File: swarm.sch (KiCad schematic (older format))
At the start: 22 parts, among them P1 USB_OTG, SW1 SW_PUSH, U1 STM32F103RETx, U2 LM3671MF-3.3, Y1 Crystal

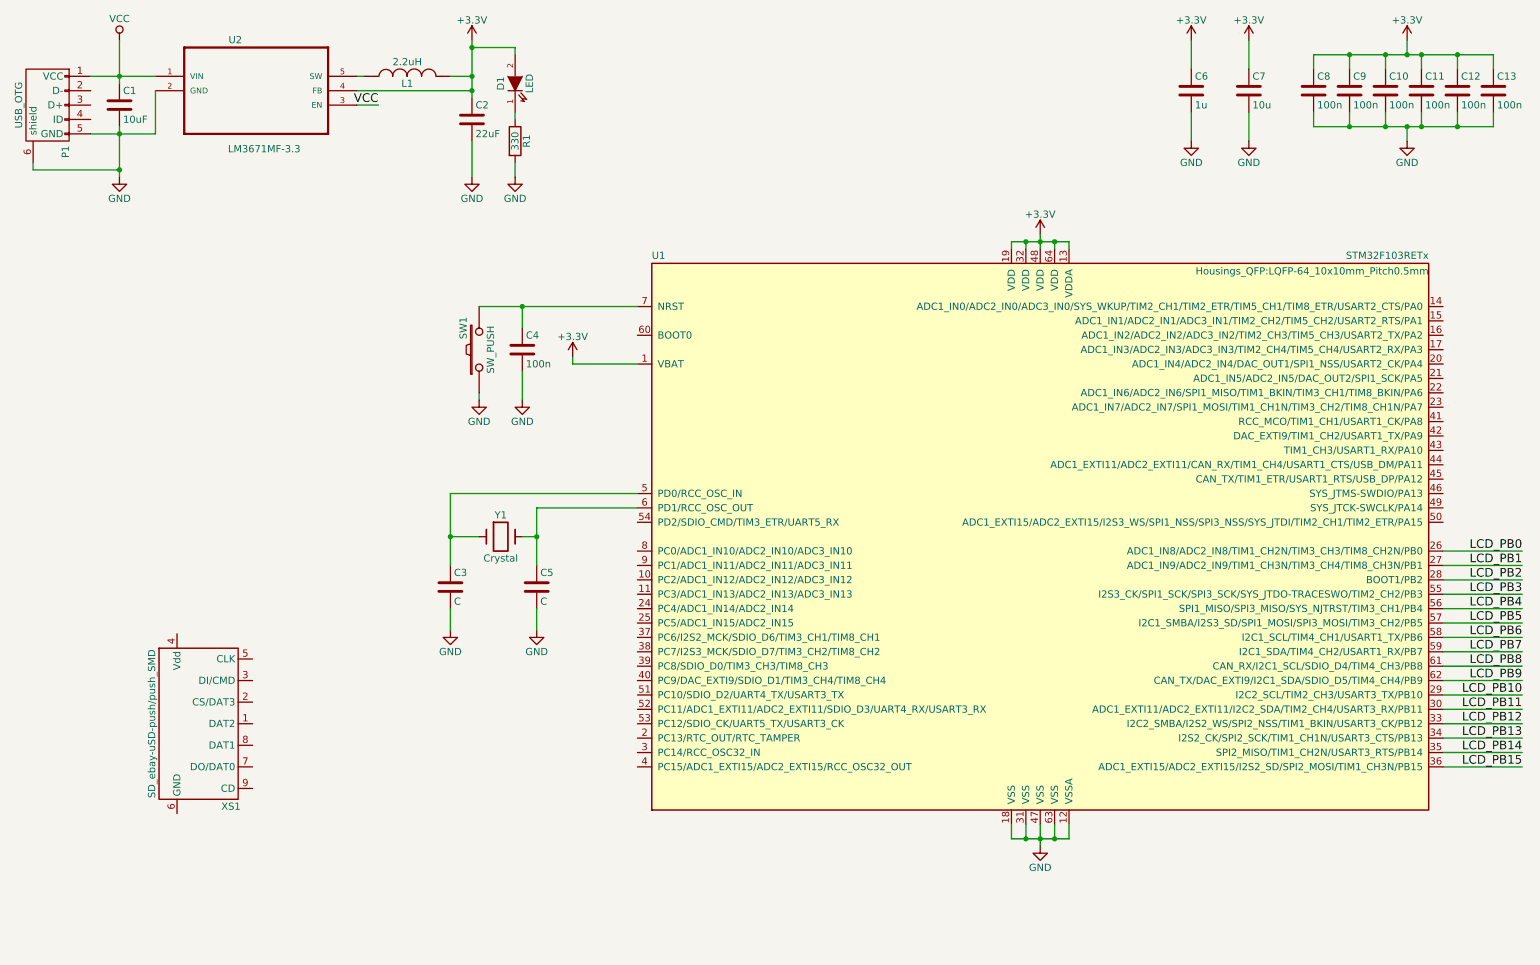
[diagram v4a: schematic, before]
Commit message: Adds Micro SD card socket connection
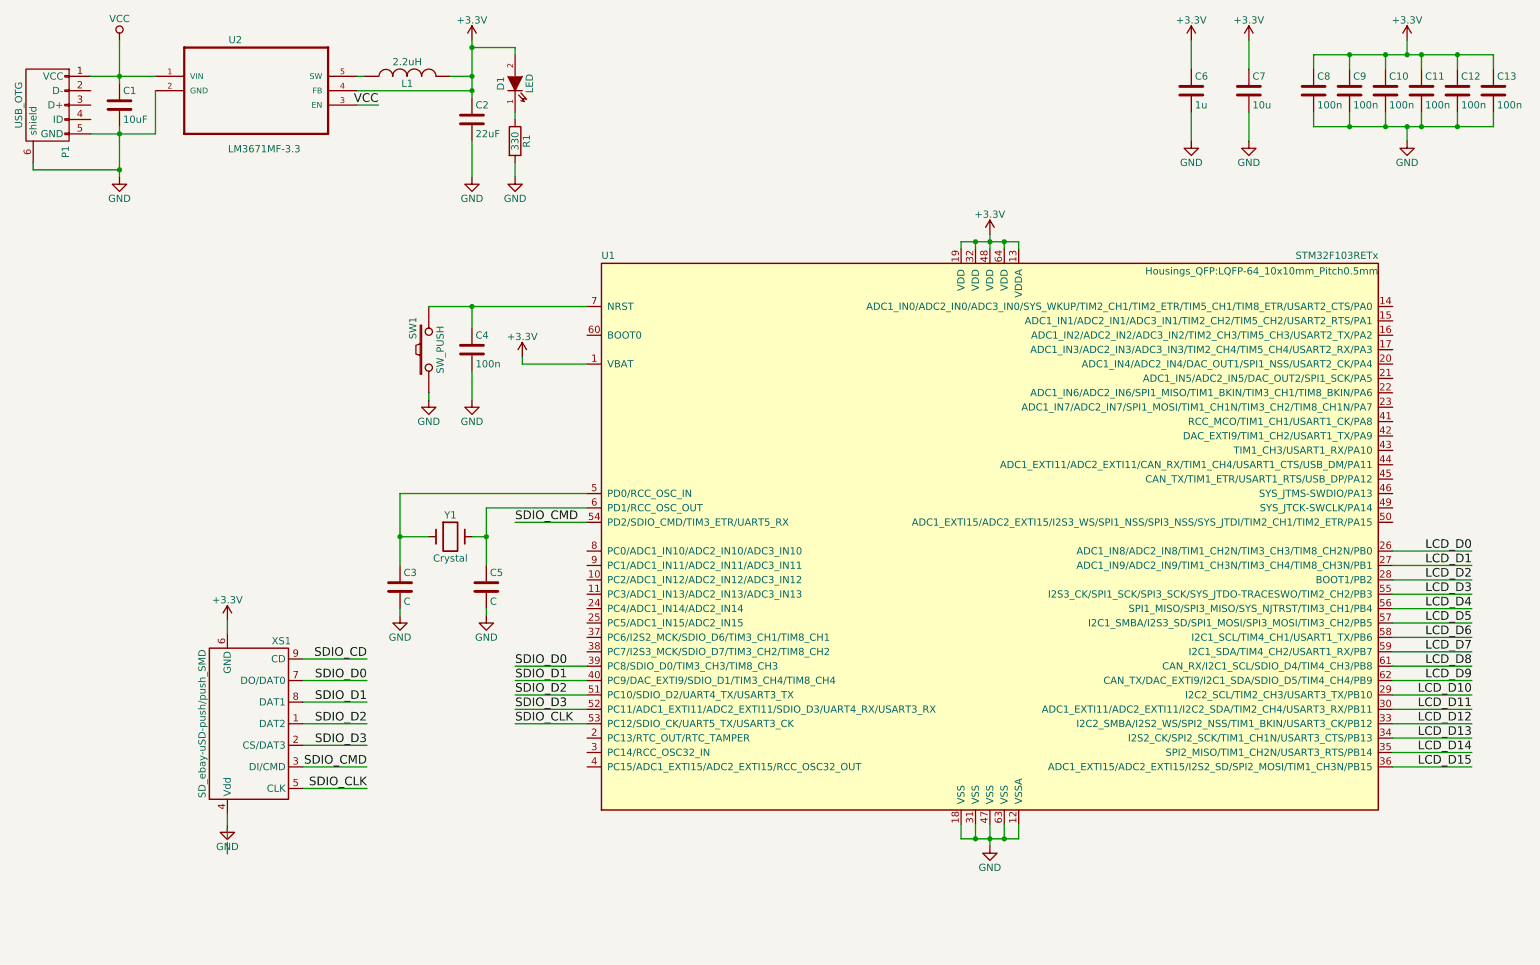
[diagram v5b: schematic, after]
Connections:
- net labels added: LCD_D0, LCD_D1, LCD_D10, LCD_D11, LCD_D12, LCD_D13, LCD_D14, LCD_D15, LCD_D2, LCD_D3, LCD_D4, LCD_D5, LCD_D6, LCD_D7, LCD_D8, LCD_D9, SDIO_CD, SDIO_CLK, SDIO_CMD, SDIO_D0, SDIO_D1, SDIO_D2, SDIO_D3
- net labels removed: LCD_PB0, LCD_PB1, LCD_PB10, LCD_PB11, LCD_PB12, LCD_PB13, LCD_PB14, LCD_PB15, LCD_PB2, LCD_PB3, LCD_PB4, LCD_PB5, LCD_PB6, LCD_PB7, LCD_PB8, LCD_PB9
- wire segments 79 -> 96
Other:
- moved on the sheet: C3, C4, C5, SW1, U1, XS1, Y1

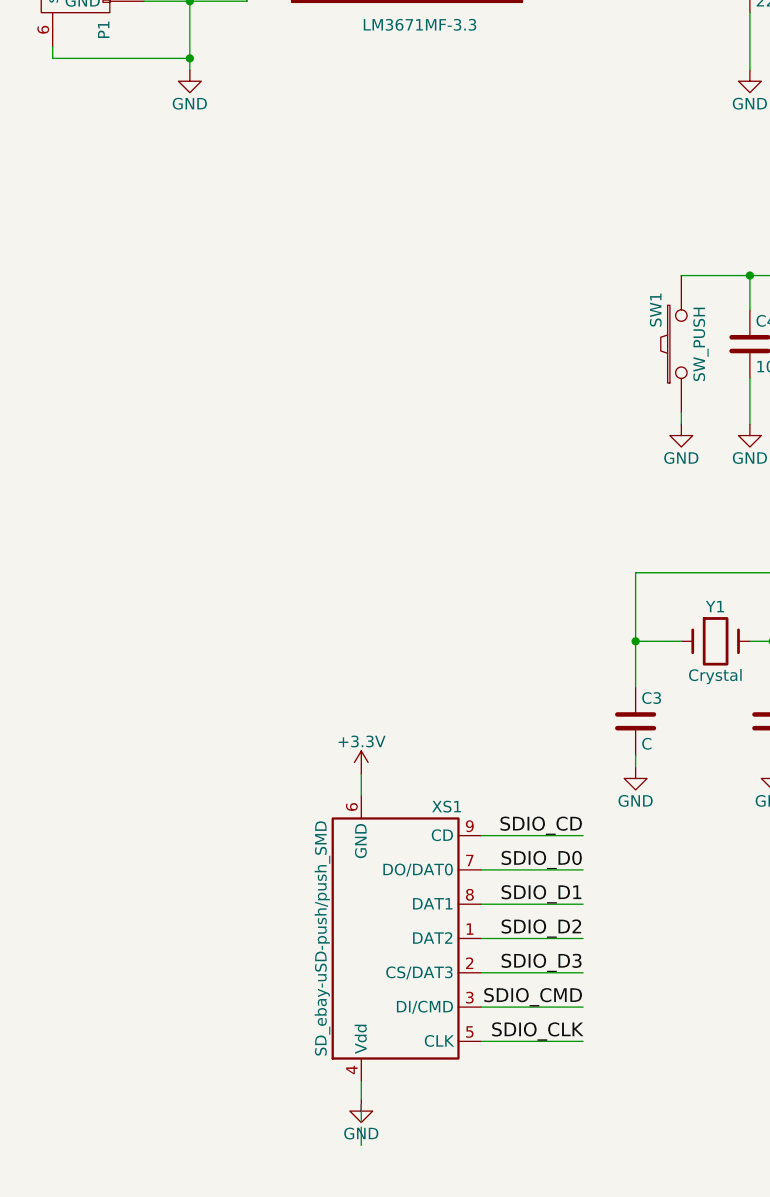
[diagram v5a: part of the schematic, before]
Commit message: Adds LCD connector 2x20 pins
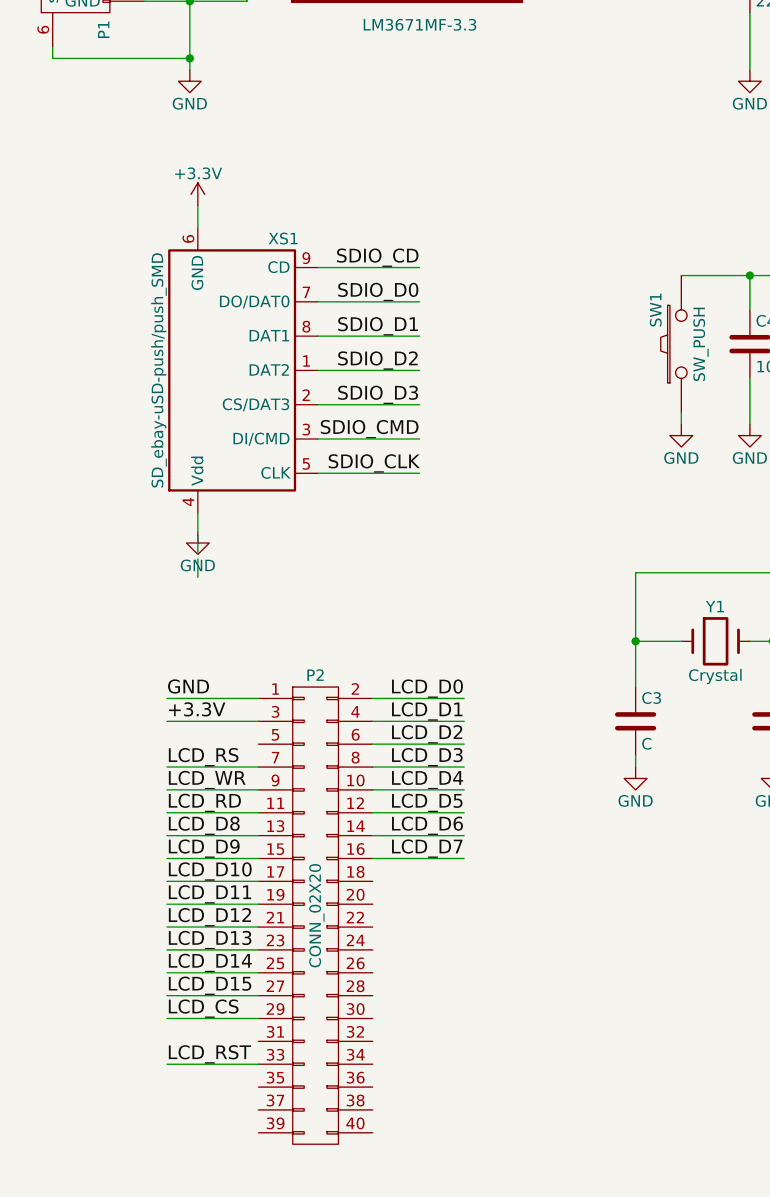
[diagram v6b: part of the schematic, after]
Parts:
- added P2: CONN_02X20, Pin_Headers:Pin_Header_Straight_2x20, symbol CONN_02X20
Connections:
- net labels added: LCD_CS, LCD_RD, LCD_RS, LCD_RST, LCD_WR
- wire segments 96 -> 119
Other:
- moved on the sheet: XS1
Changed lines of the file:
@@
 L SD_ebay-uSD-push/push_SMD XS1
 U 1 1 5840E1A5
-P 2300 5500
-F 0 "XS1" H 2525 4925 50  0000 C CNN
-F 1 "SD_ebay-uSD-push/push_SMD" V 1975 5500 50  0000 C CNN
-F 2 "volium:Conn_uSDcard" H 2300 5550 10  0001 C CNN
-F 3 "https://wiki.microduino.cc/images/c/ca/MicroSD.pdf" H 2300 5440 10  0001 C CNN
-F 4 "_" H 2300 5410 10  0001 C CNN "Manf#"
-F 5 "ebay" H 2300 5500 10  0001 C CNN "Manf"
-	1    2300 5500
+P 1585 3015
+F 0 "XS1" H 1810 2440 50  0000 C CNN
+F 1 "SD_ebay-uSD-push/push_SMD" V 1260 3015 50  0000 C CNN
+F 2 "volium:Conn_uSDcard" H 1585 3065 10  0001 C CNN
+F 3 "https://wiki.microduino.cc/images/c/ca/MicroSD.pdf" H 1585 2955 10  0001 C CNN
+F 4 "_" H 1585 2925 10  0001 C CNN "Manf#"
+F 5 "ebay" H 1585 3015 10  0001 C CNN "Manf"
+	1    1585 3015
 	1    0    0    1
 $EndComp
@@
 	4650 4100 4150 4100
 Wire Wire Line
-	2675 5050 3120 5050
-Text Label 3120 5950 2    60   ~ 0
+	1960 2565 2405 2565
+Text Label 2405 3465 2    60   ~ 0
 SDIO_CLK
 Wire Wire Line
-	2675 5200 3120 5200
-Wire Wire Line
-	2675 5350 3120 5350
-Wire Wire Line
-	2675 5500 3120 5500
-Wire Wire Line
-	2675 5650 3120 5650
-Wire Wire Line
-	2675 5800 3120 5800
-Wire Wire Line
-	2675 5950 3120 5950
-Text Label 3120 5200 2    60   ~ 0
+	1960 2715 2405 2715
+Wire Wire Line
+	1960 2865 2405 2865
+Wire Wire Line
+	1960 3015 2405 3015
+Wire Wire Line
+	1960 3165 2405 3165
+Wire Wire Line
+	1960 3315 2405 3315
+Wire Wire Line
+	1960 3465 2405 3465
+Text Label 2405 2715 2    60   ~ 0
 SDIO_D0
-Text Label 3120 5350 2    60   ~ 0
+Text Label 2405 2865 2    60   ~ 0
 SDIO_D1
-Text Label 3120 5500 2    60   ~ 0
+Text Label 2405 3015 2    60   ~ 0
 SDIO_D2
-Text Label 3120 5650 2    60   ~ 0
+Text Label 2405 3165 2    60   ~ 0
 SDIO_D3
-Text Label 3120 5800 2    60   ~ 0
+Text Label 2405 3315 2    60   ~ 0
 SDIO_CMD
-Text Label 3120 5050 2    60   ~ 0
+Text Label 2405 2565 2    60   ~ 0
 SDIO_CD
 $Comp
 L +3.3V #PWR019
 U 1 1 58424C6C
-P 2150 4780
-F 0 "#PWR019" H 2150 4630 50  0001 C CNN
-F 1 "+3.3V" H 2150 4920 50  0000 C CNN
-F 2 "" H 2150 4780 50  0000 C CNN
-F 3 "" H 2150 4780 50  0000 C CNN
-	1    2150 4780
+P 1435 2295
+F 0 "#PWR019" H 1435 2145 50  0001 C CNN
+F 1 "+3.3V" H 1435 2435 50  0000 C CNN
+F 2 "" H 1435 2295 50  0000 C CNN
+F 3 "" H 1435 2295 50  0000 C CNN
+	1    1435 2295
 	1    0    0    -1
 $EndComp
 Wire Wire Line
-	2150 4780 2150 4875
+	1435 2295 1435 2390
 $Comp
 L GND #PWR020
 U 1 1 5842512A
-P 2150 6205
-F 0 "#PWR020" H 2150 5955 50  0001 C CNN
-F 1 "GND" H 2150 6055 50  0000 C CNN
-F 2 "" H 2150 6205 50  0000 C CNN
-F 3 "" H 2150 6205 50  0000 C CNN
-	1    2150 6205
+P 1435 3720
+F 0 "#PWR020" H 1435 3470 50  0001 C CNN
+F 1 "GND" H 1435 3570 50  0000 C CNN
+F 2 "" H 1435 3720 50  0000 C CNN
+F 3 "" H 1435 3720 50  0000 C CNN
+	1    1435 3720
 	1    0    0    -1
 $EndComp
 Wire Wire Line
-	2150 6205 2150 6125
-Wire Wire Line
-	2150 6305 2150 6225
-Wire Wire Line
-	2150 6405 2150 6325
+	1435 3720 1435 3640
+Wire Wire Line
+	1435 3820 1435 3740
+Wire Wire Line
+	1435 3920 1435 3840
+$Comp
+L CONN_02X20 P2
+U 1 1 58432580
+P 1950 5400
+F 0 "P2" H 1950 6450 50  0000 C CNN
+F 1 "CONN_02X20" V 1950 5400 50  0000 C CNN
+F 2 "Pin_Headers:Pin_Header_Straight_2x20" H 1950 4450 50  0001 C CNN
+F 3 "" H 1950 4450 50  0000 C CNN
+	1    1950 5400
+	1    0    0    -1
+$EndComp
+Wire Wire Line
+	1700 4450 1300 4450
+Wire Wire Line
+	2200 4450 2600 4450
+Text Label 2600 4450 2    60   ~ 0
+LCD_D0
+Text Label 2600 4550 2    60   ~ 0
+LCD_D1
+Text Label 2600 4650 2    60   ~ 0
+LCD_D2
+Text Label 2600 4750 2    60   ~ 0
+LCD_D3
+Text Label 2600 4850 2    60   ~ 0
+LCD_D4
+Text Label 2600 4950 2    60   ~ 0
+LCD_D5
+Text Label 2600 5050 2    60   ~ 0
+LCD_D6
+Text Label 2600 5150 2    60   ~ 0
+LCD_D7
+Wire Wire Line
+	2200 4550 2600 4550
+Wire Wire Line
+	2200 4650 2600 4650
+Wire Wire Line
+	2200 4750 2600 4750
+Wire Wire Line
+	2200 4850 2600 4850
+Wire Wire Line
+	2200 4950 2600 4950
+Wire Wire Line
+	2200 5050 2600 5050
+Wire Wire Line
+	2200 5150 2600 5150
+Wire Wire Line
+	1700 5050 1300 5050
+Wire Wire Line
+	1700 5150 1300 5150
+Wire Wire Line
+	1700 5250 1300 5250
+Wire Wire Line
+	1700 5350 1300 5350
+Wire Wire Line
+	1700 5450 1300 5450
+Wire Wire Line
+	1700 5550 1300 5550
+Wire Wire Line
+	1700 5650 1300 5650
+Wire Wire Line
+	1700 5750 1300 5750
+Text Label 1300 5050 0    60   ~ 0
+LCD_D8
+Text Label 1300 5150 0    60   ~ 0
+LCD_D9
+Text Label 1300 5250 0    60   ~ 0
+LCD_D10
+Text Label 1300 5350 0    60   ~ 0
+LCD_D11
+Text Label 1300 5450 0    60   ~ 0
+LCD_D12
+Text Label 1300 5550 0    60   ~ 0
+LCD_D13
+Text Label 1300 5650 0    60   ~ 0
+LCD_D14
+Text Label 1300 5750 0    60   ~ 0
+LCD_D15
+Text Label 1300 4450 0    60   ~ 0
+GND
+Text Label 1300 4550 0    60   ~ 0
++3.3V
+Wire Wire Line
+	1700 4550 1300 4550
+Wire Wire Line
+	1700 4750 1300 4750
+Wire Wire Line
+	1700 4850 1300 4850
+Wire Wire Line
+	1700 4950 1300 4950
+Text Label 1300 4750 0    60   ~ 0
+LCD_RS
+Text Label 1300 4850 0    60   ~ 0
+LCD_WR
+Text Label 1300 4950 0    60   ~ 0
+LCD_RD
+Wire Wire Line
+	1700 5850 1300 5850
+Wire Wire Line
+	1700 6050 1300 6050
+Text Label 1300 5850 0    60   ~ 0
+LCD_CS
+Text Label 1300 6050 0    60   ~ 0
+LCD_RST
 $EndSCHEMATC

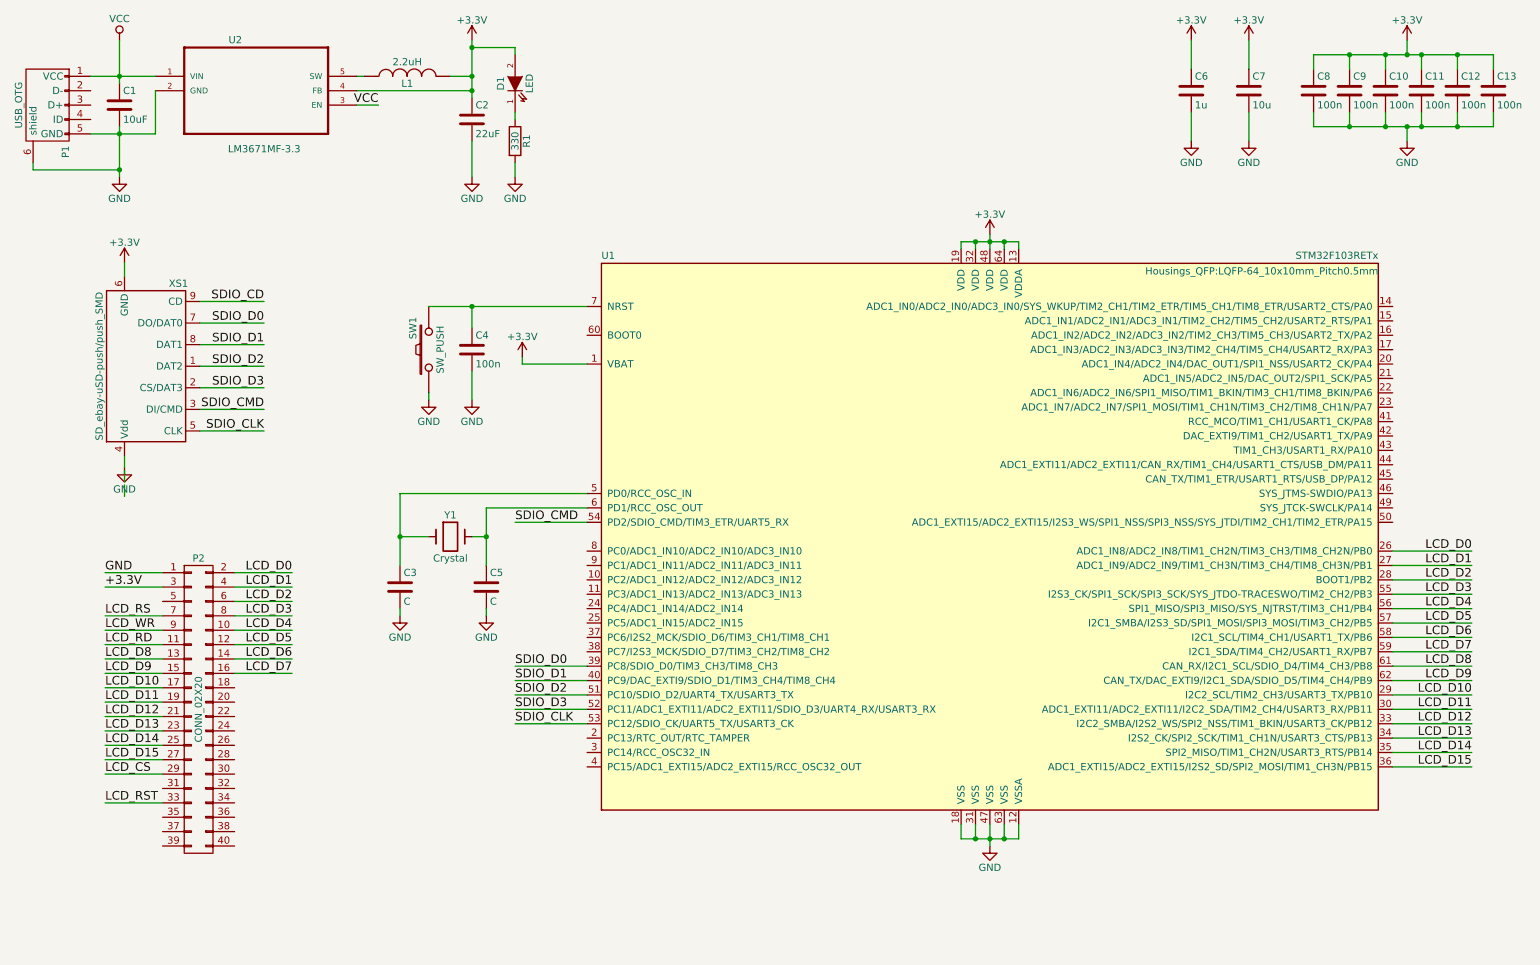
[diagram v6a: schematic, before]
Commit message: Adds Serial Wire Debug connector (5 pins) Sets up PCB layers based on Osh Park's Layer setup
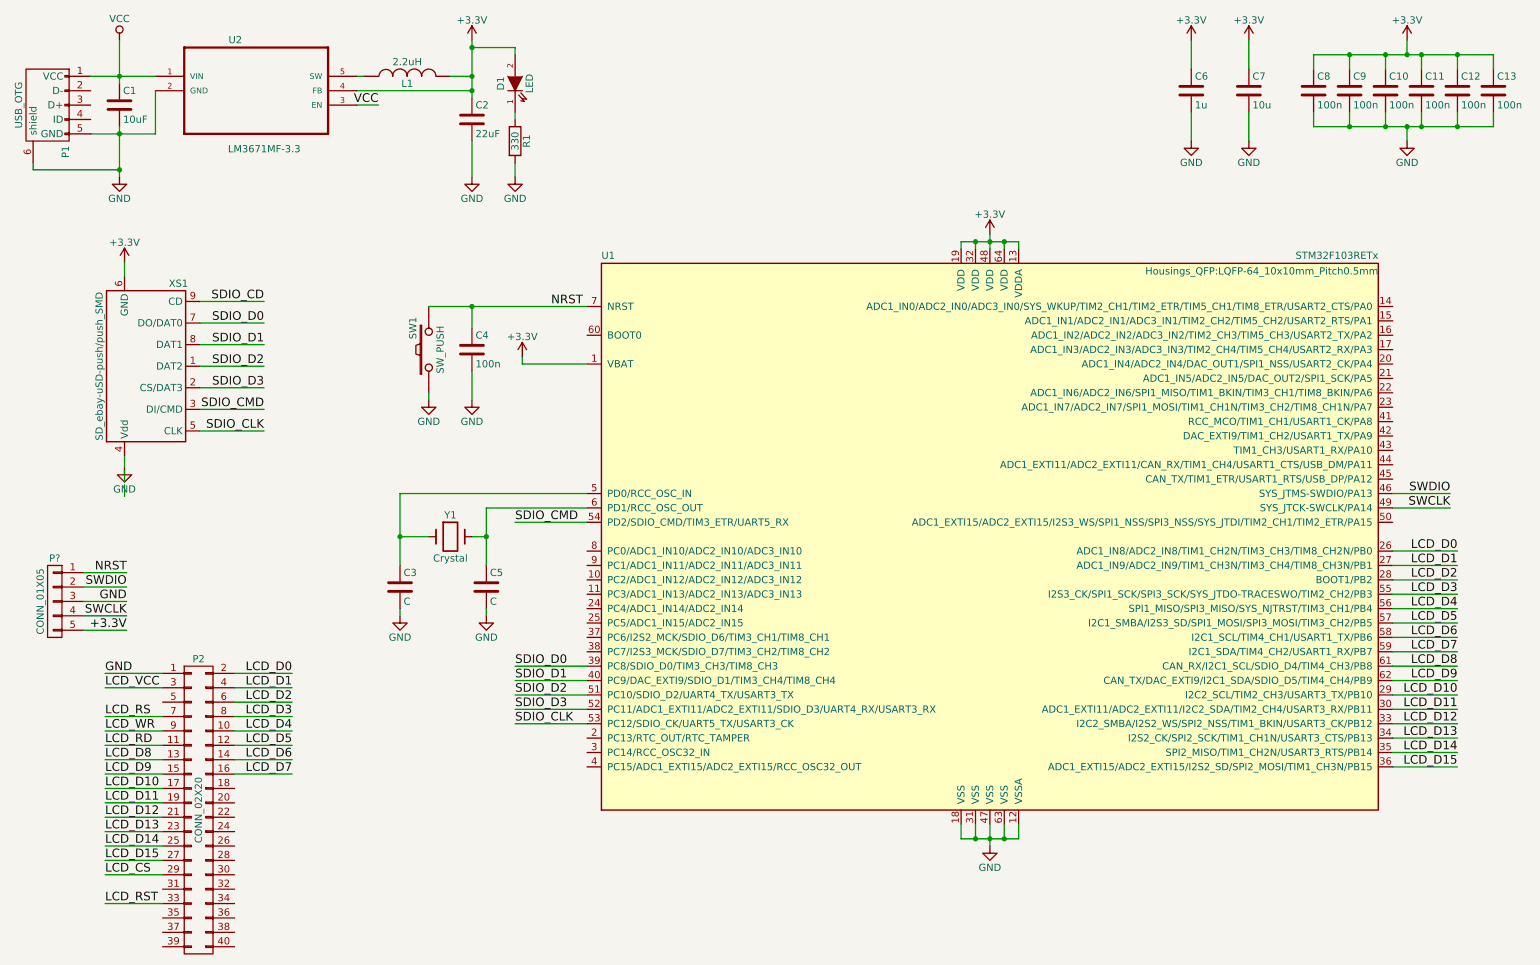
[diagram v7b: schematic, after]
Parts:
- added P?: CONN_01X05, symbol CONN_01X05
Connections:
- net +3.3V: now also P?.5 (P5); no longer P2.3 (P3)
- net GND: now also P?.3 (P3)
- net SWDIO: now reaches U1.46 (SYS_JTMS-SWDIO/PA13)
- net SWDIO: now also P?.2 (P2)
- net SWCLK: now reaches U1.49 (SYS_JTCK-SWCLK/PA14)
- net SWCLK: now also P?.4 (P4)
- net NRST: now reaches C4.1, SW1.2, U1.7 (NRST)
- net NRST: now also P?.1 (P1)
- new net LCD_VCC: P2.3 (P3)
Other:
- moved on the sheet: P2
